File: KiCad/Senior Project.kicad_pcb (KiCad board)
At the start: 4 copper layers, 25 x 60 mm, 73 parts, among them J1 USB_C_Receptacle_USB2.0_16P, J2 Screw_Terminal_01x02, J3 Screw_Terminal_01x06, Q2 IRLML0030, Q3 IRLML0030, Q4 IRLML0030, SW1 SW_Push, SW2 SW_Push, U1 ESP32-S3FH4R2, U2 TPS62162DSG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

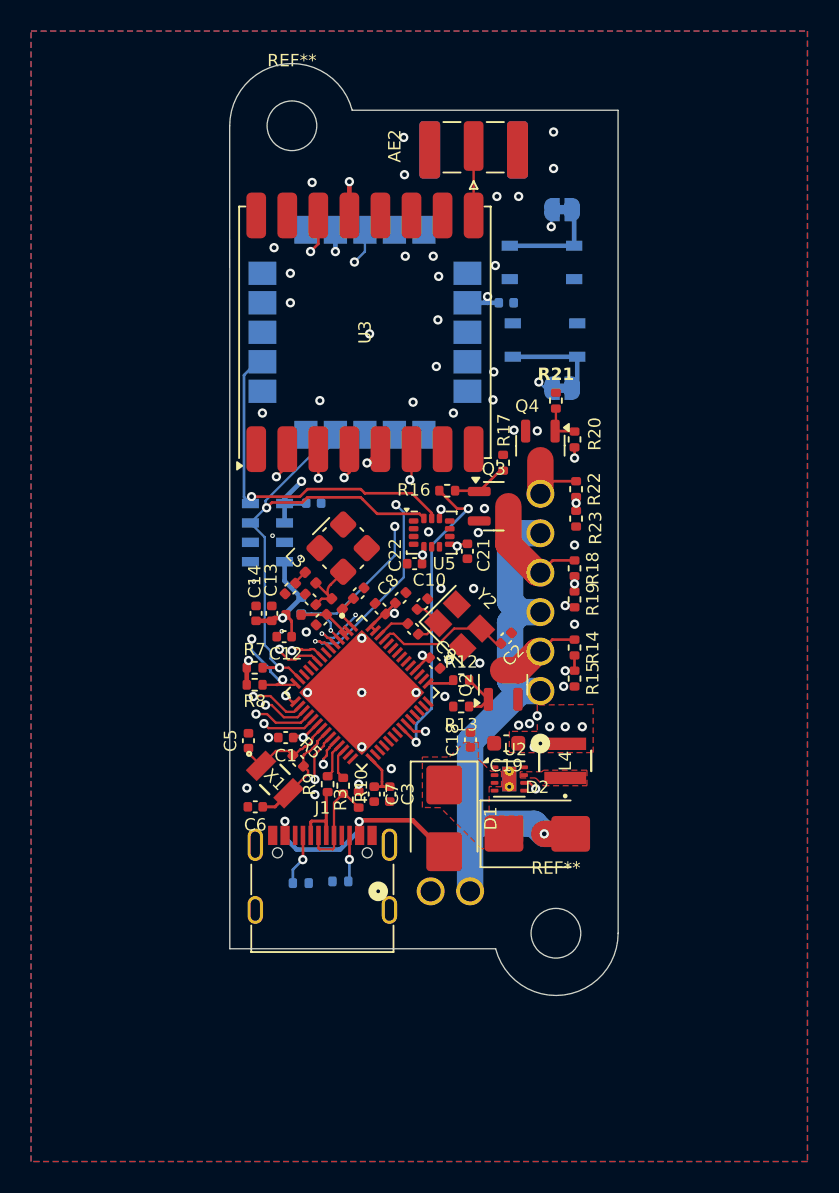
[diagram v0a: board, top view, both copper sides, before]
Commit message: fixed DRC rules, more silkscreen work
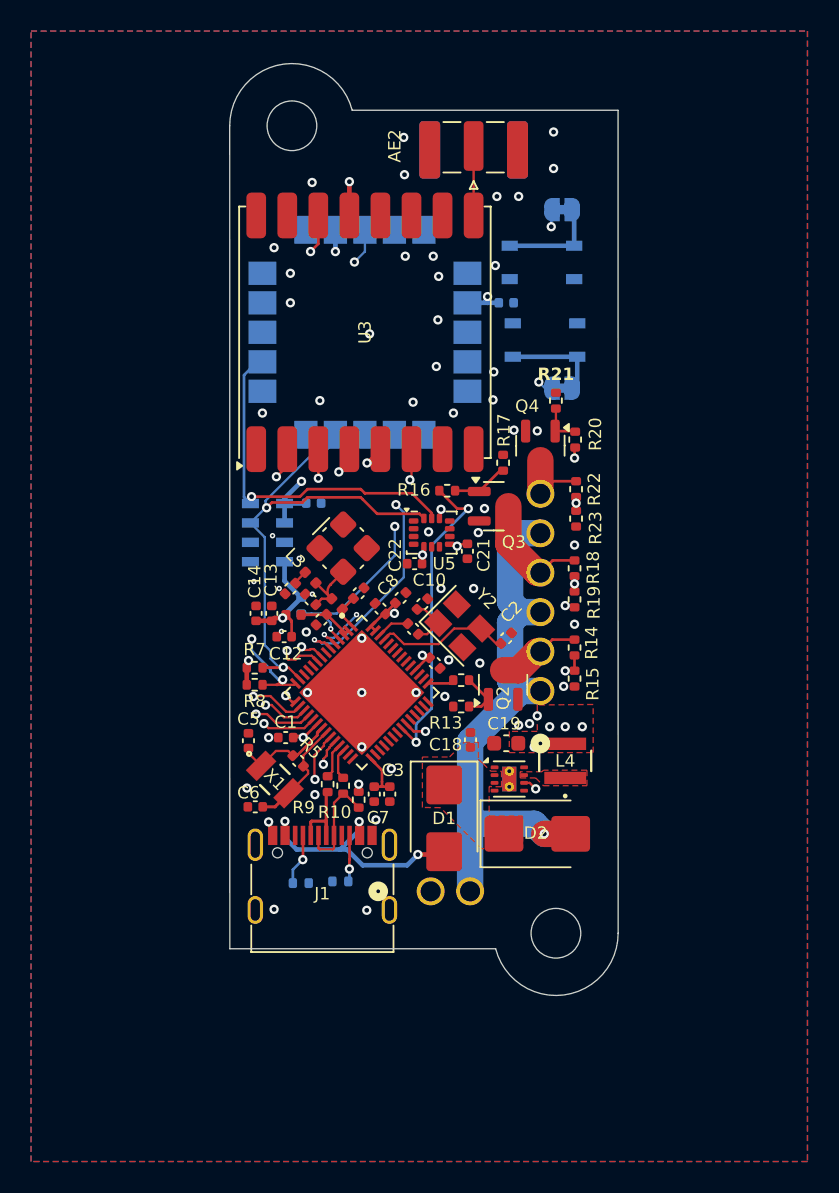
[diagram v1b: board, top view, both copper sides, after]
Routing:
- net Net-(D1-A): track 15.4 -> 16.5 mm, vias 2 -> 3
- net /GPS_Reset: track 31.7 -> 30.9 mm
- net GND: vias 53 -> 59

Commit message: adjustments to work with JLC and to match with example
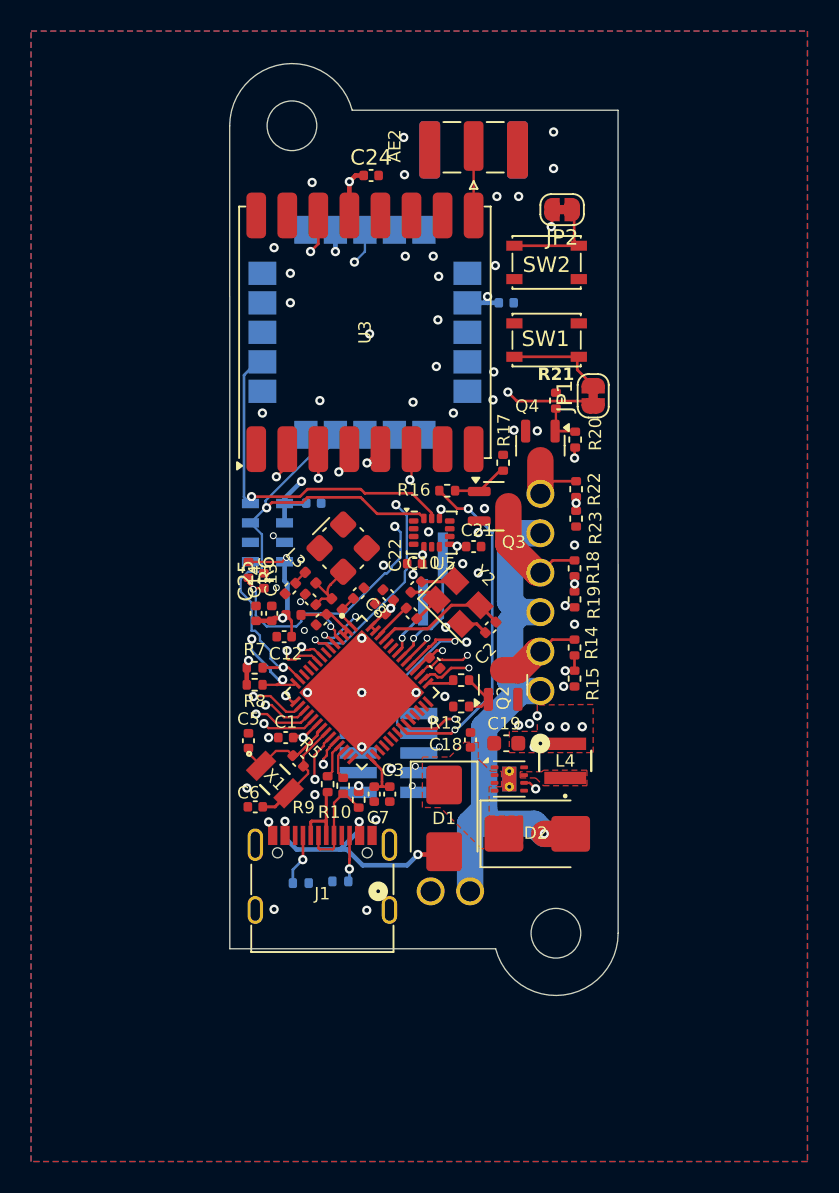
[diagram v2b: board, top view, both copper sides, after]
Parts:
- removed R11: 100k, Resistor_SMD:R_0402_1005Metric
- added C24: 1uF, Capacitor_SMD:C_0402_1005Metric, F.Cu at (84.1, 64.2)
- added C25: 1uF, Capacitor_SMD:C_0402_1005Metric, F.Cu at (77.2, 90.3)
- added J4: Conn_ARM_JTAG_SWD_10, Connector_PinHeader_1.27mm:PinHeader_2x05_P1.27mm_Vertical_SMD, B.Cu at (85.2, 101.4)
- added J5: Conn_01x02, Connector_PinHeader_1.27mm:PinHeader_1x02_P1.27mm_Vertical_SMD_Pin1Right, B.Cu at (88.1, 90.2)
- added R6: 10k, Resistor_SMD:R_0402_1005Metric, F.Cu at (76.2, 89.6)
- JP1, JP2, SW1, SW2: moved to F.Cu
- moved JP1 2.06 mm to (98.4, 78.4), turned to -90 degrees
- moved Y2 1.50 mm to (89.7, 91.7)
- moved C2 1.22 mm to (91.8, 93.3), turned to 45 degrees
- moved C10 1.17 mm to (87.0, 90.7)
- moved R4 1.00 mm to (86.7, 92.4)
- moved C8 0.82 mm to (85.2, 91.2), turned to 135 degrees
- moved C21 0.50 mm to (90.7, 88.1), turned to 0 degrees
- moved SW2 0.30 mm to (95.4, 69.8), turned to 180 degrees
- moved SW1 0.10 mm to (95.4, 74.8), turned to 0 degrees
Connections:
- net Net-(JP1-B) renamed /~{RESET}
- U1 pad 44: unconnected-(U1-GPIO39/MTCK-Pad44) -> /MTCK
- U1 pad 45: unconnected-(U1-GPIO40/MTDO-Pad45) -> /MTDO
- U1 pad 47: unconnected-(U1-GPIO41/MTDI-Pad47) -> /MTDI
- U1 pad 48: unconnected-(U1-GPIO42/MTMS-Pad48) -> /MTMS
- U1 pad 49: unconnected-(U1-GPIO43/U0TXD-Pad49) -> Net-(J5-Pin_1)
- U1 pad 50: unconnected-(U1-GPIO44/U0RXD-Pad50) -> Net-(J5-Pin_2)
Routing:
- net /~{RESET}: track 25.8 -> 47.2 mm, vias 3 -> 5
- net /MTMS: track 0.00 -> 12.9 mm, vias 0 -> 2
- net /MTDI: track 0.00 -> 12.8 mm, vias 0 -> 1
- net /MTCK: track 0.00 -> 12.6 mm, vias 0 -> 2
- net /MTDO: track 0.00 -> 11.7 mm, vias 0 -> 2
- net Net-(J5-Pin_1): track 0.00 -> 7.93 mm, vias 0 -> 1
- net Net-(J5-Pin_2): track 0.00 -> 4.05 mm, vias 0 -> 1
- net GND: track 0.00 -> 4.02 mm
- net /Sense 2: track 26.1 -> 29.0 mm
- net /Sense 3: track 26.8 -> 29.6 mm
- net +3V3: track 63.7 -> 66.4 mm, vias 18 -> 19
- net /Pyro GPIO 2: track 20.1 -> 21.9 mm
- net /SDA: track 33.8 -> 35.5 mm
- net /GPS_Reset: track 30.9 -> 31.6 mm

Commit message: prepare to move barometer to front
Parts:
- JP1, JP2: moved to B.Cu
- R1, R2: moved to F.Cu
- moved R1 8.07 mm to (87.3, 112.1)
- moved R2 7.49 mm to (89.2, 112.1)
- moved JP2 3.64 mm to (95.4, 69.9), turned to -90 degrees
- moved JP1 0.22 mm to (98.6, 78.3)
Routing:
- net Net-(J1-CC2): track 2.99 -> 10.6 mm, vias 1 -> 2
- net Net-(J1-CC1): track 3.34 -> 10.5 mm, vias 1 -> 2
- net Net-(JP2-B): track 35.3 -> 31.5 mm
- net Net-(JP2-A): track 6.65 -> 4.67 mm, vias 0 -> 1
- net Net-(JP1-A): track 6.48 -> 7.34 mm, vias 0 -> 1
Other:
- outline, holes or cut-outs redrawn

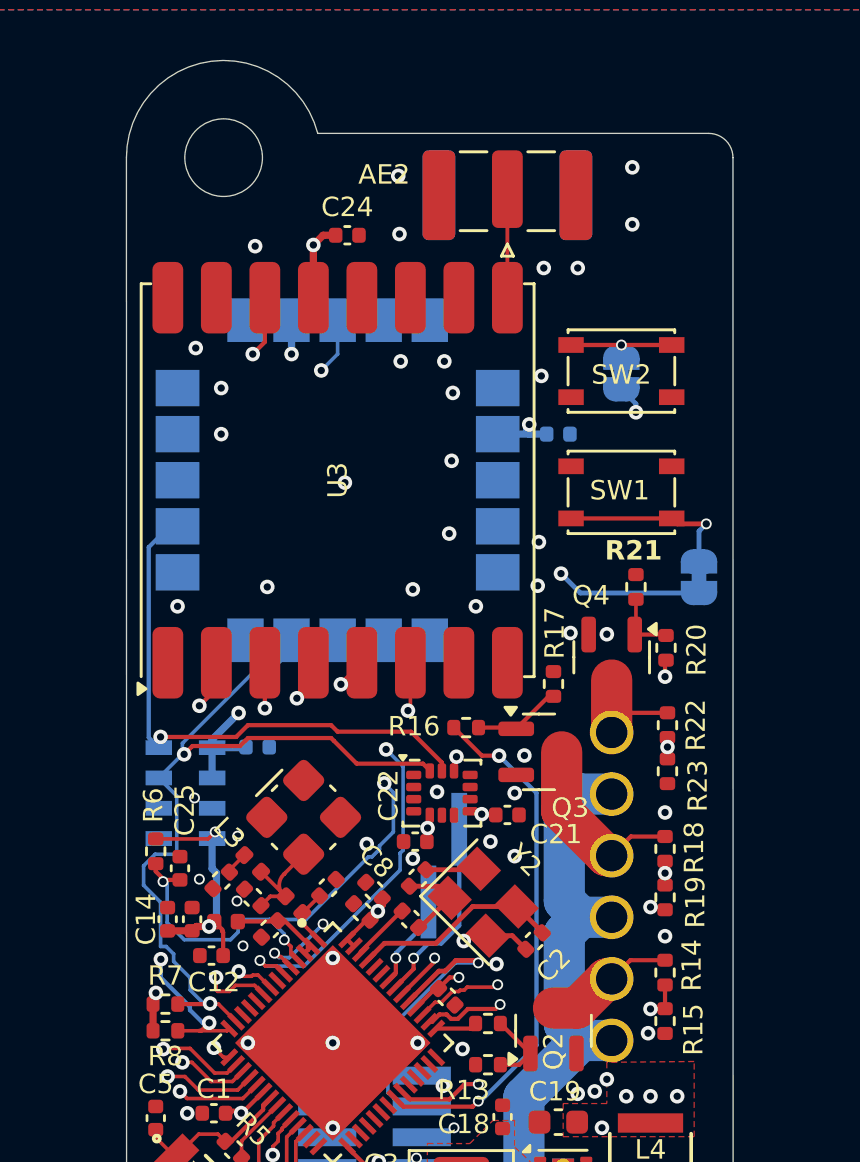
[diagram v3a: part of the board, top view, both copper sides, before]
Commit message: move barometer to front
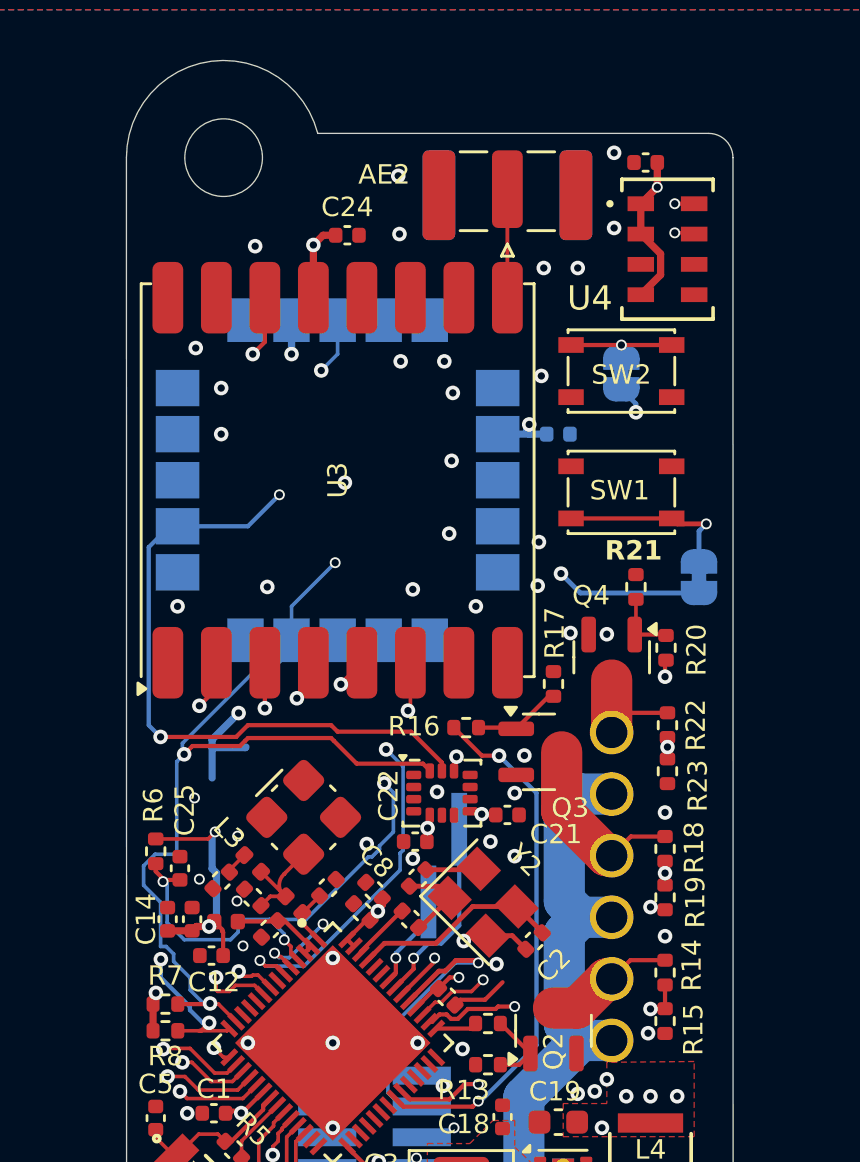
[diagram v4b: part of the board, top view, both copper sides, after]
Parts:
- C20, U4: moved to F.Cu
- moved U4 30.0 mm to (97.3, 64.8), turned to 0 degrees
- moved C20 28.9 mm to (96.4, 61.2), turned to 180 degrees
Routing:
- net /SCL: track 38.7 -> 65.1 mm, vias 3 -> 5
- net /SDA: track 35.5 -> 59.4 mm, vias 2 -> 4
- net +3V3: track 66.4 -> 72.8 mm, vias 19 -> 20
- net GND: track 4.02 -> 6.37 mm
- net /MTCK: track 12.6 -> 13.8 mm
- net /MTDO: track 11.7 -> 11.0 mm

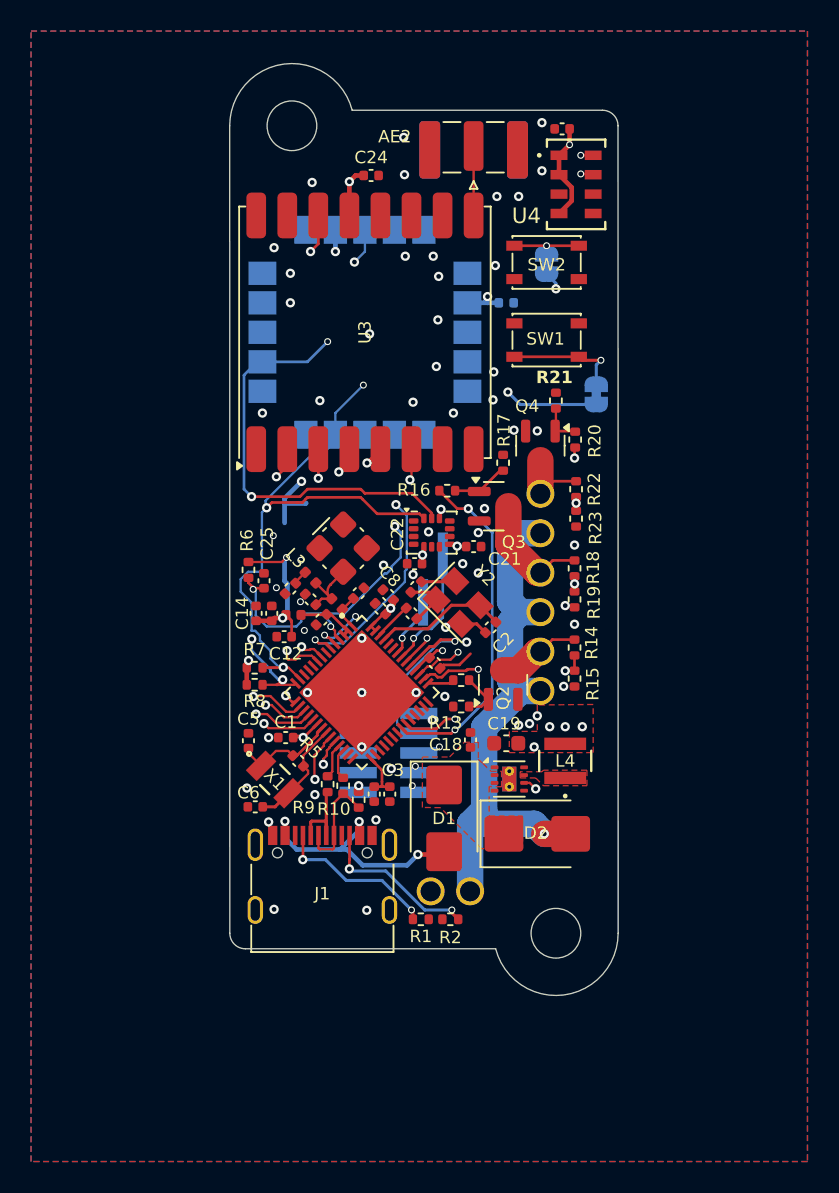
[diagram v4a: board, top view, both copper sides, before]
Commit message: add JLC assembly tooling holes
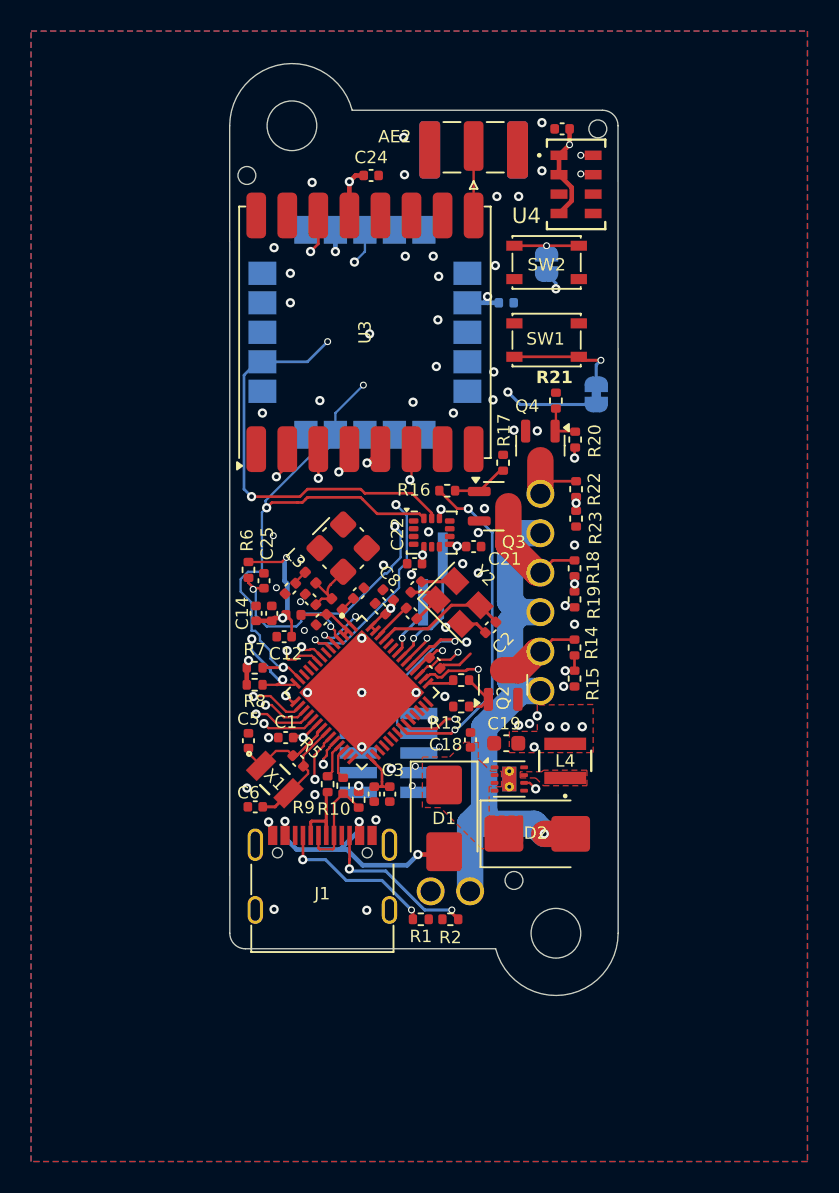
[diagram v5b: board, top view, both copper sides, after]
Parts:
- added REF**: ToolingHole_1.152mm, MountingHole:ToolingHole_1.152mm, F.Cu at (76.1, 64.2)
- added REF**: ToolingHole_1.152mm, MountingHole:ToolingHole_1.152mm, F.Cu at (98.7, 61.2)
- added REF**: ToolingHole_1.152mm, MountingHole:ToolingHole_1.152mm, F.Cu at (93.3, 109.6)
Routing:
- net +3V3: track 72.8 -> 68.3 mm, vias 20 -> 19

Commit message: finalize board
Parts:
- added D3: LED, LED_SMD:LED_0603_1608Metric, B.Cu at (93.8, 81.9)
- added D5: LED, LED_SMD:LED_0603_1608Metric, B.Cu at (77.9, 103.5)
- added R11: 1, Resistor_SMD:R_2512_6332Metric, B.Cu at (91.9, 102.8)
- added R24: R_Small, Resistor_SMD:R_0603_1608Metric, B.Cu at (97.0, 80.9)
- added R25: 100k, Resistor_SMD:R_0402_1005Metric, F.Cu at (84.9, 84.1)
- added R27: R_Small, Resistor_SMD:R_0603_1608Metric, B.Cu at (79.5, 103.5)
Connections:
- J3 pad 1: +BATT -> Net-(J3-Pin_1)
- J3 pad 3: +BATT -> Net-(J3-Pin_1)
- J3 pad 5: +BATT -> Net-(J3-Pin_1)
- U1 pad 10: unconnected-(U1-GPIO5-Pad10) -> /POWER_LED
- U6 pad 7: unconnected-(U6-TIMEPULSE-Pad7) -> Net-(D3-A)
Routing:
- net +BATT: track 36.1 -> 11.9 mm
- net Net-(J3-Pin_1): track 0.00 -> 21.0 mm
- net /POWER_LED: track 0.00 -> 9.17 mm, vias 0 -> 1
- net Net-(D3-A): track 0.00 -> 7.99 mm
- net Net-(D3-K): track 0.00 -> 1.99 mm
- net Net-(D5-K): track 0.00 -> 1.62 mm
- net +3V3: track 68.3 -> 69.0 mm, vias 19 -> 20
- net /RADIO_RST: track 21.1 -> 21.7 mm
- net GND: vias 59 -> 62
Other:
- board text added: "2025-04-06"
- board text added: "BOOT"
- board text added: "Mark 1"
- board text added: "OSU AIAA ASDT"
- board text added: "RESET"
